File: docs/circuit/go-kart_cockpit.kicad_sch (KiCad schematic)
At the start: 24 parts, among them X2 Bluetooth-Modul, X3 2x13, X4 2x13

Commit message: WIP: planning cockpit pins
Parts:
- removed R1, R2, R3, R4, R5, R6, R7, R8, R9: 10k, symbol Device:R
- removed R10: 1k, symbol Device:R
- removed S1: Blinker links (D6R), symbol Switch:SW_MEC_5E
- removed S2: Fernlicht (D6R), symbol Switch:SW_MEC_5E
- removed S3: kein Licht/Tagfahr-/Abblendlicht (D6R), symbol Switch:SW_MEC_5E
- removed S4: Hupe (D6R), symbol Switch:SW_MEC_5E
- removed S5: Blinker rechts (D6R), symbol Switch:SW_MEC_5E
- removed S6: Warnblinker, Button_Switch_THT:SW_Slide-03_Wuerth-WS-SLTV_10x2.5x6.4_P2.54mm, symbol Switch:SW_Wuerth_450301014042
- removed S7: Gang runter (D6R), symbol Switch:SW_MEC_5E
- removed S8: Gang hoch (D6R), symbol Switch:SW_MEC_5E
- removed S9: Start/Aus/Rückwärts, symbol Switch:SW_SPDT_MSM
- added D1: 1N4004, Diode_THT:D_DO-41_SOD81_P10.16mm_Horizontal, symbol Diode:1N4004
- added Q1: TIP120, Package_TO_SOT_THT:TO-220-3_Vertical, symbol Transistor_BJT:TIP120
- added R13, R14: 10k, symbol Device:R
- added R15: R, symbol Device:R
- added S10: Start/Aus/Rückwärts, symbol Switch:SW_SPDT_MSM
- added X1: Display (male), Connector_IDC:IDC-Header_2x03_P2.54mm_Horizontal, symbol Connector_Generic:Conn_02x03_Odd_Even
- added X1: 24V Hupe (-), symbol Connector:Conn_01x02_Pin
- added X1: Taster links (male), Connector_IDC:IDC-Header_2x05_P2.54mm_Horizontal, symbol Connector_Generic:Conn_02x05_Odd_Even
- added X5: Taster rechts (male), Connector_IDC:IDC-Header_2x05_P2.54mm_Horizontal, symbol Connector_Generic:Conn_02x05_Odd_Even
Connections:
- net GND: now also R13.2, R14.2
- net Vcc (5V): now also S10.2 (3)
- new net: Q1.1 (B), R15.1
- new net: D1.1 (K), Q1.2 (C), X1.1 (Pin_1)
- new net: D1.2 (A), Q1.3 (E), X1.2 (Pin_2)
- new net: R13.1, S10.3 (4)
- new net: R14.1, S10.1
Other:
- note added: "Hupe(-)"
- moved on the sheet: X3, X4

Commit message: WIP: circuit
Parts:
- removed D1: 1N4004, Diode_THT:D_DO-41_SOD81_P10.16mm_Horizontal, symbol Diode:1N4004
- removed X1: 24V Hupe (-), symbol Connector:Conn_01x02_Pin
- removed X4: 2x13, symbol Connector_Generic:Conn_02x13_Odd_Even
- added J1: 2x13, Connector_PinHeader_2.54mm:PinHeader_2x13_P2.54mm_Vertical, symbol Connector_Generic:Conn_02x13_Odd_Even
- added R1: 1N4148, Diode_THT:D_DO-35_SOD27_P7.62mm_Horizontal, symbol Diode:1N4148
- added R7: 1N4004, Diode_THT:D_DO-41_SOD81_P10.16mm_Horizontal, symbol Diode:1N4004
- added X1: ISP-6, Connector_IDC:IDC-Header_2x03_P2.54mm_Horizontal, symbol Connector:AVR-ISP-6
- added X6: 24V Hupe, Connector_AMASS:AMASS_XT60PW-M_1x02_P7.20mm_Horizontal, symbol Connector:Conn_01x02_Pin
- J2: renamed from X3; footprint (none) -> Connector_PinHeader_2.54mm:PinHeader_2x13_P2.54mm_Vertical
- Q1: footprint Package_TO_SOT_THT:TO-220-3_Vertical -> Package_TO_SOT_THT:TO-220F-3_Horizontal_TabDown
- R2: renamed from R13; footprint (none) -> Resistor_THT:R_Axial_DIN0204_L3.6mm_D1.6mm_P7.62mm_Horizontal
- R3: renamed from R11; footprint (none) -> Resistor_THT:R_Axial_DIN0204_L3.6mm_D1.6mm_P7.62mm_Horizontal
- R4: renamed from R12; footprint (none) -> Resistor_THT:R_Axial_DIN0204_L3.6mm_D1.6mm_P7.62mm_Horizontal
- R5: renamed from R14; footprint (none) -> Resistor_THT:R_Axial_DIN0204_L3.6mm_D1.6mm_P7.62mm_Horizontal
- R6: renamed from R15; value R -> 470 10%; footprint (none) -> Resistor_THT:R_Axial_DIN0204_L3.6mm_D1.6mm_P7.62mm_Horizontal
- S1: renamed from S10; footprint (none) -> Connector_AMASS:AMASS_MR30PW-FB_1x03_P3.50mm_Horizontal
- X2: footprint (none) -> Connector_JST:JST_EH_S4B-EH_1x04_P2.50mm_Horizontal
- renumbered X1 to X3, X5 to X4, X1 to X5
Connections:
- net GND: now also Q1.3 (E), X5.5 (Pin_5), J1.5 (Pin_5), J1.6 (Pin_6), J1.7 (Pin_7), J1.8 (Pin_8), X1.6 (GND)
- net Vcc (5V): now also J2.9 (Pin_9), X5.1 (Pin_1), J1.9 (Pin_9), R1.1 (K); no longer J2.1 (Pin_1), J2.2 (Pin_2), J2.3 (Pin_3), J2.4 (Pin_4)
- net PD3_TXD1: now reaches X5.2 (Pin_2)
- net PD3_TXD1: now also J1.16 (Pin_16)
- net PD2_RXD1: now reaches X5.6 (Pin_6)
- net PD2_RXD1: now also J1.15 (Pin_15)
- net PB7_OC0A: now reaches R6.2
- net PB7_OC0A: now also J2.11 (Pin_11)
- net PE0_RXD0: now reaches X2.3 (Pin_3)
- net PE0_RXD0: now also J2.25 (Pin_25)
- net at Q1.2 (C): now also R7.2 (A), X6.2 (Pin_2)
- net PE1_TXD0: now reaches R3.1
- net PE1_TXD0: now also J2.26 (Pin_26)
- net PB1_SCK: now reaches J2.14 (Pin_14)
- net PB1_SCK: now also X1.3 (SCK)
- net PB2_MOSI: now reaches J2.15 (Pin_15)
- net PB2_MOSI: now also X1.4 (MOSI)
- net PB3_MISO: now reaches J2.16 (Pin_16)
- net PB3_MISO: now also X1.1 (MISO)
- net PE4_LED_LightSwitch: now reaches J2.21 (Pin_21)
- net PE2_LED_BlinkerL: now reaches J2.23 (Pin_23)
- net PE3_LED_BlinkerR: now reaches J2.24 (Pin_24)
- new net: R1.2 (A), X1.2 (VCC)
- new net +24V: J1.1 (Pin_1), J1.2 (Pin_2), J1.3 (Pin_3), J1.4 (Pin_4), J2.1 (Pin_1), J2.2 (Pin_2), J2.3 (Pin_3), J2.4 (Pin_4), R7.1 (K), X6.1 (Pin_1)
- new net PC2_SW_BlinkerL: J1.24 (Pin_24)
- new net PC3_SW_BlinkerR: J1.25 (Pin_25)
- new net PD4_SW_LightSwitch: J1.17 (Pin_17)
- new net /RESET: J1.26 (Pin_26), X1.5 (~{RST})
- no-connect marks 0 -> 2
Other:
- note added: "Hupe(+)"
- note added: "I1=3,5A"
- moved on the sheet: J2, Q1, R2, R3, R4, R5, R6, S1, X2, X3, X4, X5

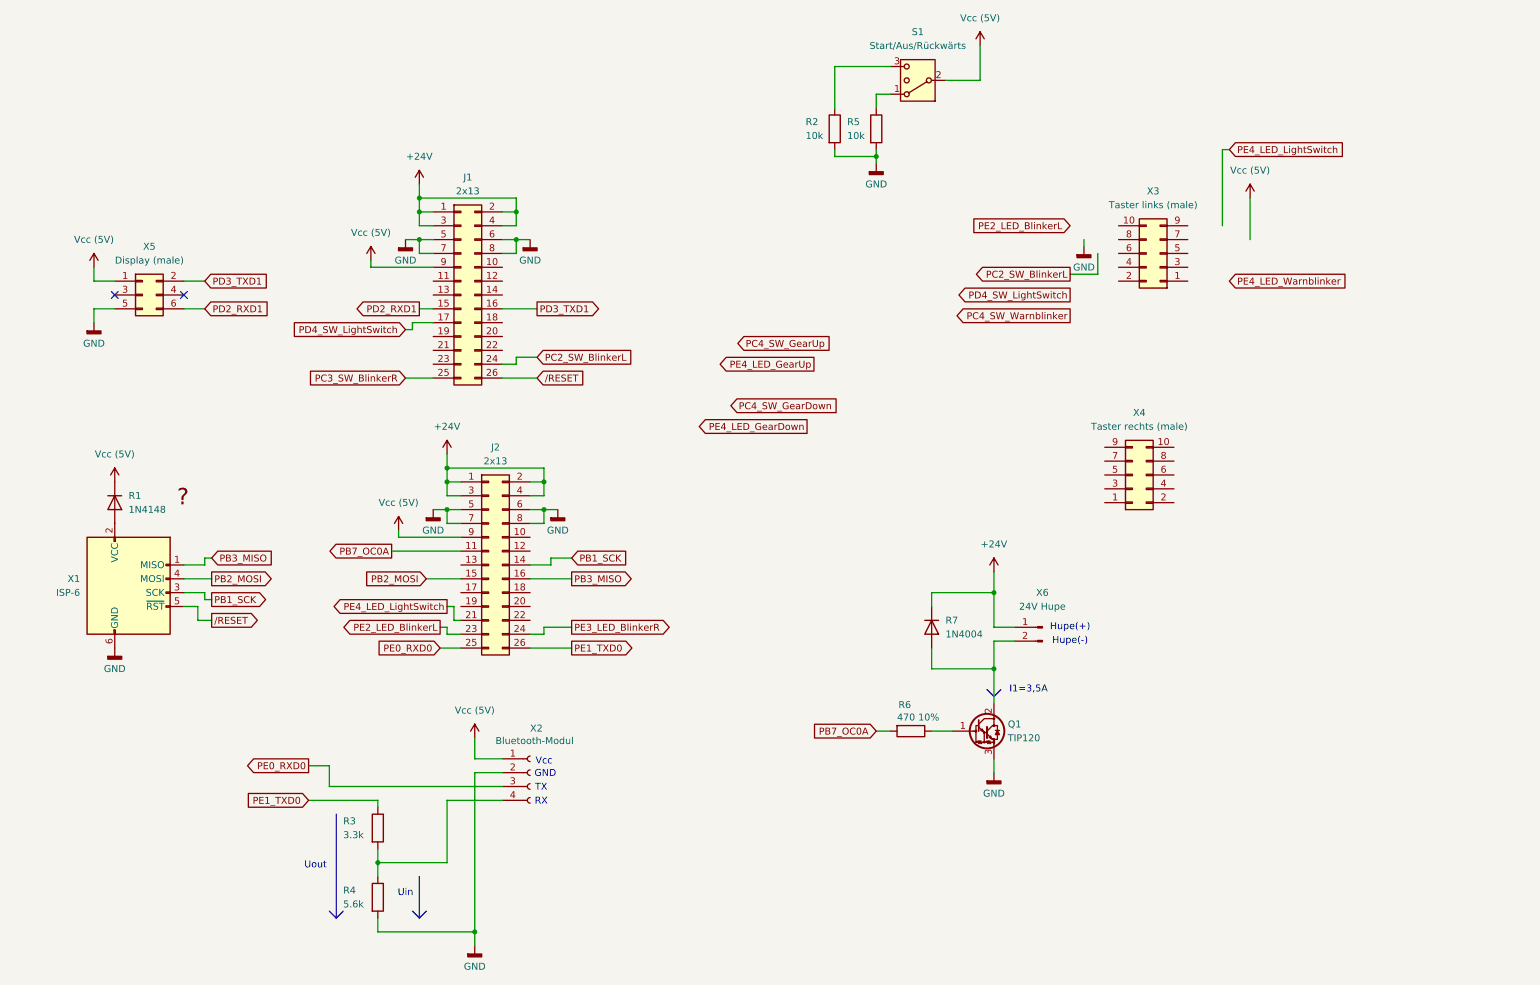
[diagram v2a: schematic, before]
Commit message: feat(circuit): use internal pull up resistors
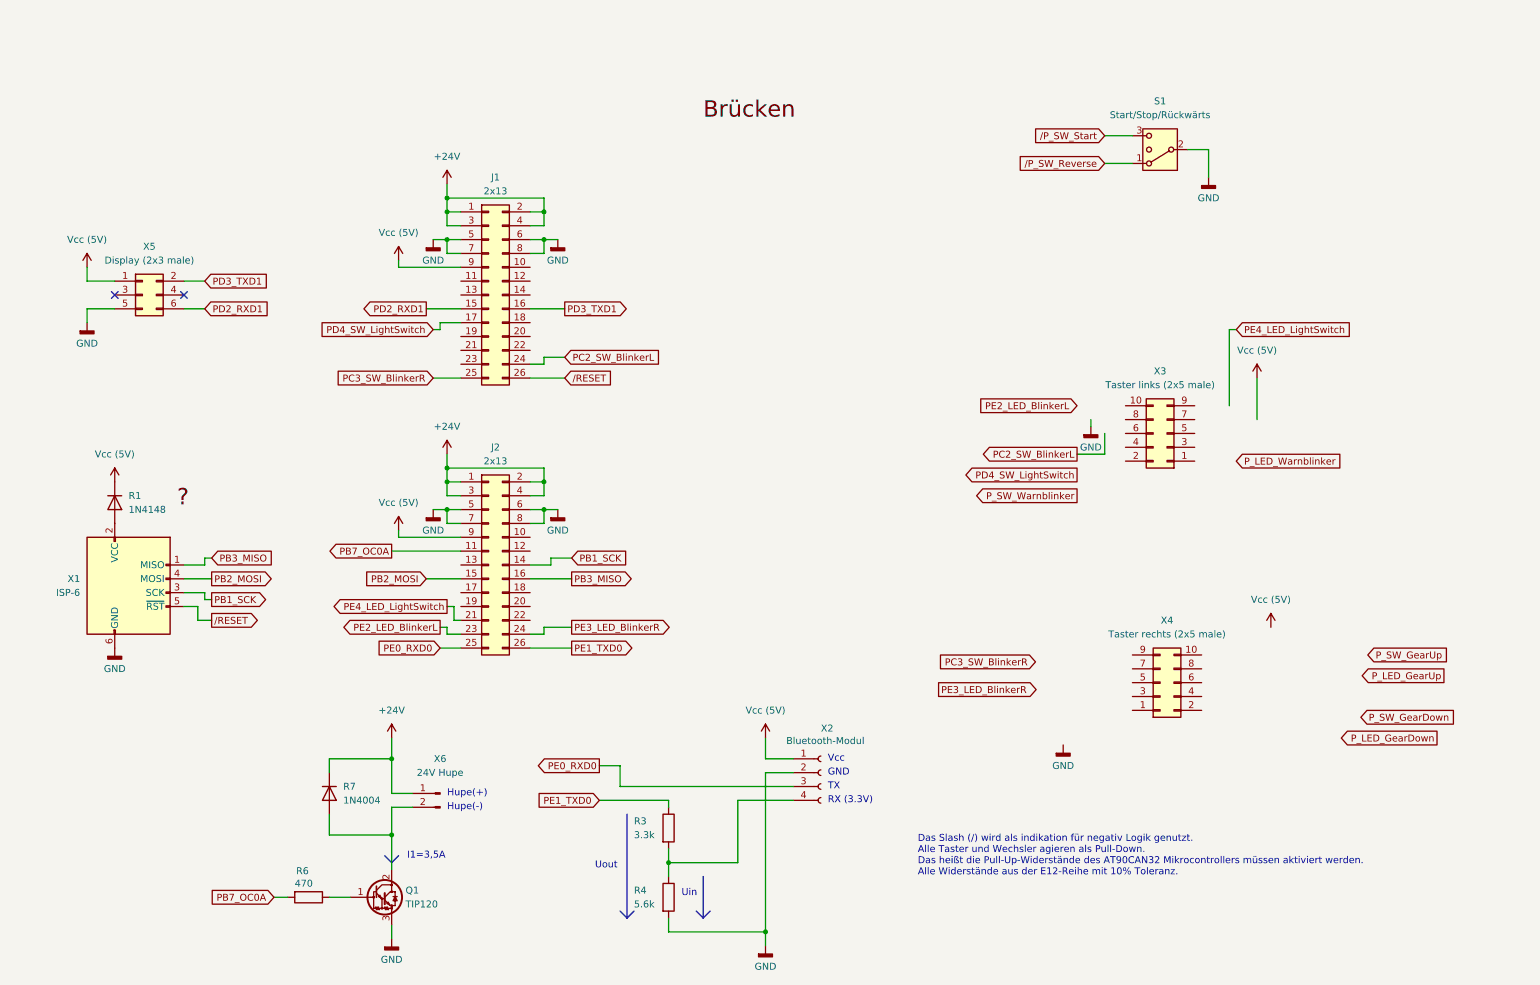
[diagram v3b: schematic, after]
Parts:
- removed R2, R5: 10k, Resistor_THT:R_Axial_DIN0204_L3.6mm_D1.6mm_P7.62mm_Horizontal, symbol Device:R
- R6: value 470 10% -> 470
- S1: value Start/Aus/Rückwärts -> Start/Stop/Rückwärts
- X3: value Taster links (male) -> Taster links (2x5 male)
- X4: value Taster rechts (male) -> Taster rechts (2x5 male)
- X5: value Display (male) -> Display (2x3 male)
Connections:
- net GND: now also S1.2 (3)
- net Vcc (5V): no longer S1.2 (3)
- net /P_SW_Start: now reaches S1.3 (4)
- net /P_SW_Reverse: now reaches S1.1
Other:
- note added: "Das Slash (/) wird als indikation für negativ Logik genutzt. Alle Taster und Wechsler agieren als Pull-Down. Das heißt die Pull-Up-Widerstände des AT90CAN32 Mikrocontrollers müssen aktiviert werden. Alle Widerstände aus der E12-Reihe mit 10% Toleranz."
- note added: "RX (3.3V)"
- note removed: "RX"
- moved on the sheet: J1, Q1, R3, R4, R6, R7, S1, X2, X3, X4, X6

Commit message: feat: circuit before rework with larger plate
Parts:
- removed R1: 1N4148, Diode_THT:D_DO-35_SOD27_P7.62mm_Horizontal, symbol Diode:1N4148
- removed R7: 1N4004, Diode_THT:D_DO-41_SOD81_P10.16mm_Horizontal, symbol Diode:1N4004
- removed X1: ISP-6, Connector_IDC:IDC-Header_2x03_P2.54mm_Horizontal, symbol Connector:AVR-ISP-6
- removed X6: 24V Hupe, Connector_AMASS:AMASS_XT60PW-M_1x02_P7.20mm_Horizontal, symbol Connector:Conn_01x02_Pin
- added D1: LED, symbol Device:LED
- added R1: 1N5817, Diode_THT:D_DO-41_SOD81_P10.16mm_Horizontal, symbol Diode:1N5817
- added R2: 1N4936, Diode_THT:D_DO-41_SOD81_P10.16mm_Horizontal, symbol Diode:1N4936
- added R6: 100-120, symbol Device:R
- added R7: 3k, symbol Device:R
- added SW1: SW_MEC_5E, symbol Switch:SW_MEC_5E
- added X1: AVR-ISP-10, Connector_IDC:IDC-Header_2x05_P2.54mm_Horizontal, symbol Connector:AVR-ISP-10
- added X3: 24V Hupe, TerminalBlock_Phoenix:TerminalBlock_Phoenix_MKDS-1,5-3-5.08_1x03_P5.08mm_Horizontal, symbol Connector:Conn_01x03_Pin
- X4: renamed from S1; footprint Connector_AMASS:AMASS_MR30PW-FB_1x03_P3.50mm_Horizontal -> TerminalBlock_Phoenix:TerminalBlock_Phoenix_MKDS-1,5-3-5.08_1x03_P5.08mm_Horizontal
- X7: renamed from X3; value Taster links (2x5 male) -> Taster links (male)
- renumbered R6 to R3, R3 to R4, R4 to R5, X5 to X2, X2 to X5, X4 to X6
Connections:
- net /P_SW_Reverse is gone; now on net /PE5_SW_Reverse: X4.1
- net /P_SW_Start is gone; now on net /PE3_SW_Start: X4.3 (4)
- net +24V: now also R2.1 (K), X3.2 (Pin_2)
- net GND: now also X6.7 (Pin_7), X7.8 (Pin_8), D1.1 (K), R7.2, X1.10 (GND), X1.4 (GND), X1.6 (GND), X1.8 (GND)
- net PB1_SCK: now also X1.7 (SCK)
- net PB2_MOSI: now also X1.1 (MOSI)
- net PB3_MISO: now also X1.9 (MISO)
- net PC3_SW_BlinkerR: now also X6.1 (Pin_1)
- net PD2_RXD1: now also J2.25 (Pin_25); no longer J1.15 (Pin_15)
- net PD3_TXD1: now also J2.26 (Pin_26); no longer J1.16 (Pin_16)
- net PE0_RXD0: now also J1.15 (Pin_15); no longer J2.25 (Pin_25)
- net PE1_TXD0: now also J1.16 (Pin_16); no longer J2.26 (Pin_26)
- net P_LED_GearDown: now also X6.10 (Pin_10)
- net P_LED_GearUp: now also X6.9 (Pin_9)
- net P_LED_Warnblinker: now also X7.10 (Pin_10)
- net P_SW_GearDown: now also X6.3 (Pin_3)
- net P_SW_GearUp: now also X6.5 (Pin_5)
- net P_SW_Warnblinker: now also X7.6 (Pin_6)
- net Vcc (5V): now also X6.8 (Pin_8), X7.7 (Pin_7), R1.1 (K), SW1.1, SW1.2; no longer J1.9 (Pin_9)
- net /RESET: now also X1.5 (~{RST})
- net at Q1.2 (C): now also R2.2 (A), X3.3 (Pin_3)
- net P_LED_BlinkerR: now reaches X6.2 (Pin_2)
- net /PE5_SW_Reverse: now reaches J2.22 (Pin_22)
- net P_LED_BlinkerL: now reaches X7.1 (Pin_1)
- net P_SW_BlinkerL: now reaches X7.2 (Pin_2)
- net P_SW_LightSwitch: now reaches X7.4 (Pin_4)
- net P_LED_LightSwitch: now reaches X7.9 (Pin_9)
- net PE3_LED_BlinkerR renamed /PE3_SW_Start
- new net: D1.2 (A), R6.2
- new net: R1.2 (A), X1.2 (VCC)
- new net LED*: R6.1
- new net SW*: R7.1, SW1.3 (K), SW1.4 (A)
- no-connect marks 2 -> 7
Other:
- note added: "Innenbeschaltung der Tasterplatinen"
- moved on the sheet: J1, J2, Q1, R3, R4, R5, X4, X5, X6, X7

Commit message: WIP: circuit
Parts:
- added R8, R9: 100, Resistor_THT:R_Axial_DIN0204_L3.6mm_D1.6mm_P7.62mm_Horizontal, symbol Device:R
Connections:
- net Vcc (5V): now also J1.9 (Pin_9)
- net /PE3_SW_Start: now also R8.1; no longer X4.3 (4)
- net /PE5_SW_Reverse: now also R9.1; no longer X4.1
- new net: R8.2, X4.3 (4)
- new net: R9.2, X4.1
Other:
- moved on the sheet: X4
